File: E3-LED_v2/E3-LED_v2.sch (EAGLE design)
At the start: 4 parts

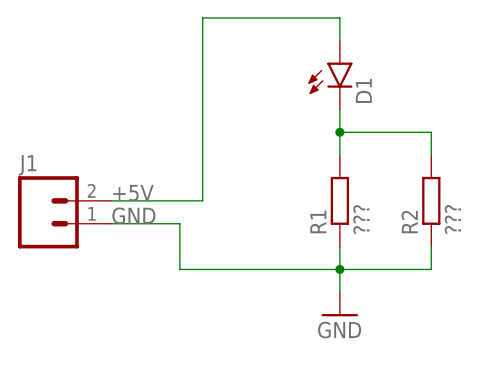
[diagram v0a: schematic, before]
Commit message: Updated BOM and schematic of v2 board with final LED and resistor choice.
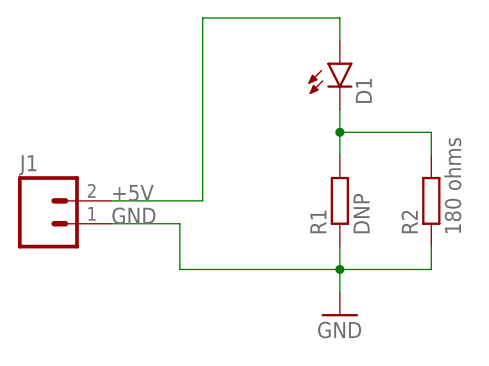
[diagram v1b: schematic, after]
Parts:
- R1: value ??? -> DNP
- R2: value ??? -> 180 ohms
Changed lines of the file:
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@@
 <grid distance="0.1" unitdist="inch" unit="inch" style="lines" multiple="1" display="no" altdistance="0.01" altunitdist="inch" altunit="inch"/>
 <layers>
-<layer number="1" name="Top" color="4" fill="1" visible="yes" active="no"/>
-<layer number="2" name="Route2" color="1" fill="3" visible="yes" active="no"/>
-<layer number="3" name="Route3" color="4" fill="3" visible="yes" active="no"/>
-<layer number="4" name="Route4" color="1" fill="4" visible="yes" active="no"/>
-<layer number="5" name="Route5" color="4" fill="4" visible="yes" active="no"/>
-<layer number="6" name="Route6" color="1" fill="8" visible="yes" active="no"/>
-<layer number="7" name="Route7" color="4" fill="8" visible="yes" active="no"/>
-<layer number="8" name="Route8" color="1" fill="2" visible="yes" active="no"/>
-<layer number="9" name="Route9" color="4" fill="2" visible="yes" active="no"/>
-<layer number="10" name="Route10" color="1" fill="7" visible="yes" active="no"/>
-<layer number="11" name="Route11" color="4" fill="7" visible="yes" active="no"/>
-<layer number="12" name="Route12" color="1" fill="5" visible="yes" active="no"/>
-<layer number="13" name="Route13" color="4" fill="5" visible="yes" active="no"/>
-<layer number="14" name="Route14" color="1" fill="6" visible="yes" active="no"/>
-<layer number="15" name="Route15" color="4" fill="6" visible="yes" active="no"/>
-<layer number="16" name="Bottom" color="1" fill="1" visible="yes" active="no"/>
-<layer number="17" name="Pads" color="2" fill="1" visible="yes" active="no"/>
-<layer number="18" name="Vias" color="2" fill="1" visible="yes" active="no"/>
-<layer number="19" name="Unrouted" color="6" fill="1" visible="yes" active="no"/>
-<layer number="20" name="Dimension" color="15" fill="1" visible="yes" active="no"/>
-<layer number="21" name="tPlace" color="7" fill="1" visible="yes" active="no"/>
-<layer number="22" name="bPlace" color="7" fill="1" visible="yes" active="no"/>
-<layer number="23" name="tOrigins" color="15" fill="1" visible="yes" active="no"/>
-<layer number="24" name="bOrigins" color="15" fill="1" visible="yes" active="no"/>
-<layer number="25" name="tNames" color="7" fill="1" visible="yes" active="no"/>
-<layer number="26" name="bNames" color="7" fill="1" visible="yes" active="no"/>
-<layer number="27" name="tValues" color="7" fill="1" visible="yes" active="no"/>
-<layer number="28" name="bValues" color="7" fill="1" visible="yes" active="no"/>
+<layer number="1" name="Top" color="4" fill="1" visible="no" active="no"/>
+<layer number="2" name="Route2" color="1" fill="3" visible="no" active="no"/>
+<layer number="3" name="Route3" color="4" fill="3" visible="no" active="no"/>
+<layer number="4" name="Route4" color="1" fill="4" visible="no" active="no"/>
+<layer number="5" name="Route5" color="4" fill="4" visible="no" active="no"/>
+<layer number="6" name="Route6" color="1" fill="8" visible="no" active="no"/>
+<layer number="7" name="Route7" color="4" fill="8" visible="no" active="no"/>
+<layer number="8" name="Route8" color="1" fill="2" visible="no" active="no"/>
+<layer number="9" name="Route9" color="4" fill="2" visible="no" active="no"/>
+<layer number="10" name="Route10" color="1" fill="7" visible="no" active="no"/>
+<layer number="11" name="Route11" color="4" fill="7" visible="no" active="no"/>
+<layer number="12" name="Route12" color="1" fill="5" visible="no" active="no"/>
+<layer number="13" name="Route13" color="4" fill="5" visible="no" active="no"/>
+<layer number="14" name="Route14" color="1" fill="6" visible="no" active="no"/>
+<layer number="15" name="Route15" color="4" fill="6" visible="no" active="no"/>
+<layer number="16" name="Bottom" color="1" fill="1" visible="no" active="no"/>
+<layer number="17" name="Pads" color="2" fill="1" visible="no" active="no"/>
+<layer number="18" name="Vias" color="2" fill="1" visible="no" active="no"/>
+<layer number="19" name="Unrouted" color="6" fill="1" visible="no" active="no"/>
+<layer number="20" name="Dimension" color="15" fill="1" visible="no" active="no"/>
+<layer number="21" name="tPlace" color="7" fill="1" visible="no" active="no"/>
+<layer number="22" name="bPlace" color="7" fill="1" visible="no" active="no"/>
+<layer number="23" name="tOrigins" color="15" fill="1" visible="no" active="no"/>
+<layer number="24" name="bOrigins" color="15" fill="1" visible="no" active="no"/>
+<layer number="25" name="tNames" color="7" fill="1" visible="no" active="no"/>
+<layer number="26" name="bNames" color="7" fill="1" visible="no" active="no"/>
+<layer number="27" name="tValues" color="7" fill="1" visible="no" active="no"/>
+<layer number="28" name="bValues" color="7" fill="1" visible="no" active="no"/>
 <layer number="29" name="tStop" color="7" fill="3" visible="no" active="no"/>
 <layer number="30" name="bStop" color="7" fill="6" visible="no" active="no"/>
@@
 <layer number="35" name="tGlue" color="7" fill="4" visible="no" active="no"/>
 <layer number="36" name="bGlue" color="7" fill="5" visible="no" active="no"/>
-<layer number="37" name="tTest" color="7" fill="1" visible="yes" active="no"/>
-<layer number="38" name="bTest" color="7" fill="1" visible="yes" active="no"/>
+<layer number="37" name="tTest" color="7" fill="1" visible="no" active="no"/>
+<layer number="38" name="bTest" color="7" fill="1" visible="no" active="no"/>
 <layer number="39" name="tKeepout" color="4" fill="11" visible="no" active="no"/>
 <layer number="40" name="bKeepout" color="1" fill="11" visible="no" active="no"/>
@@
 <layer number="44" name="Drills" color="7" fill="1" visible="no" active="no"/>
 <layer number="45" name="Holes" color="7" fill="1" visible="no" active="no"/>
-<layer number="46" name="Milling" color="3" fill="1" visible="yes" active="no"/>
-<layer number="47" name="Measures" color="7" fill="1" visible="yes" active="no"/>
-<layer number="48" name="Document" color="7" fill="1" visible="yes" active="no"/>
-<layer number="49" name="Reference" color="7" fill="1" visible="yes" active="no"/>
-<layer number="50" name="dxf" color="7" fill="1" visible="yes" active="no"/>
-<layer number="51" name="tDocu" color="7" fill="1" visible="yes" active="no"/>
-<layer number="52" name="bDocu" color="7" fill="1" visible="yes" active="no"/>
-<layer number="53" name="tGND_GNDA" color="7" fill="9" visible="yes" active="no"/>
-<layer number="54" name="bGND_GNDA" color="1" fill="9" visible="yes" active="no"/>
-<layer number="56" name="wert" color="7" fill="1" visible="yes" active="no"/>
-<layer number="57" name="tCAD" color="7" fill="1" visible="yes" active="no"/>
-<layer number="59" name="tCarbon" color="7" fill="1" visible="yes" active="no"/>
-<layer number="60" name="bCarbon" color="7" fill="1" visible="yes" active="no"/>
+<layer number="46" name="Milling" color="3" fill="1" visible="no" active="no"/>
+<layer number="47" name="Measures" color="7" fill="1" visible="no" active="no"/>
+<layer number="48" name="Document" color="7" fill="1" visible="no" active="no"/>
+<layer number="49" name="Reference" color="7" fill="1" visible="no" active="no"/>
+<layer number="50" name="dxf" color="7" fill="1" visible="no" active="no"/>
+<layer number="51" name="tDocu" color="7" fill="1" visible="no" active="no"/>
+<layer number="52" name="bDocu" color="7" fill="1" visible="no" active="no"/>
+<layer number="53" name="tGND_GNDA" color="7" fill="9" visible="no" active="no"/>
+<layer number="54" name="bGND_GNDA" color="1" fill="9" visible="no" active="no"/>
+<layer number="56" name="wert" color="7" fill="1" visible="no" active="no"/>
+<layer number="57" name="tCAD" color="7" fill="1" visible="no" active="no"/>
+<layer number="59" name="tCarbon" color="7" fill="1" visible="no" active="no"/>
+<layer number="60" name="bCarbon" color="7" fill="1" visible="no" active="no"/>
 <layer number="90" name="Modules" color="5" fill="1" visible="yes" active="yes"/>
 <layer number="91" name="Nets" color="2" fill="1" visible="yes" active="yes"/>
@@
 <parts>
 <part name="FRAME1" library="frames" deviceset="LETTER_L" device=""/>
-<part name="R1" library="eagle-ltspice" deviceset="R" device="0204/7" value="???"/>
+<part name="R1" library="eagle-ltspice" deviceset="R" device="0204/7" value="DNP"/>
 <part name="GND1" library="SparkFun-Aesthetics" deviceset="GND" device=""/>
 <part name="D1" library="SparkFun-LED" deviceset="LED" device="5MM"/>
 <part name="J1" library="SparkFun-Connectors" deviceset="M02" device="PTH"/>
-<part name="R2" library="eagle-ltspice" deviceset="R" device="R0603" value="???"/>
+<part name="R2" library="eagle-ltspice" deviceset="R" device="R0603" value="180 ohms"/>
 </parts>
 <sheets>

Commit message: Tweaked silk.
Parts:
- removed R1: DNP, eagle-ltspice:R0204/7
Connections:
- net GND: no longer R1.1
- net N$3: no longer R1.2
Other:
- moved on the sheet: R2
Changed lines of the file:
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@@
 <parts>
 <part name="FRAME1" library="frames" deviceset="LETTER_L" device=""/>
-<part name="R1" library="eagle-ltspice" deviceset="R" device="0204/7" value="DNP"/>
 <part name="GND1" library="SparkFun-Aesthetics" deviceset="GND" device=""/>
 <part name="D1" library="SparkFun-LED" deviceset="LED" device="5MM"/>
@@
 <instance part="FRAME1" gate="G$1" x="0" y="0"/>
 <instance part="FRAME1" gate="G$2" x="147.32" y="0"/>
-<instance part="R1" gate="G$1" x="83.82" y="99.06" rot="R90"/>
 <instance part="GND1" gate="1" x="83.82" y="86.36"/>
 <instance part="D1" gate="G$1" x="83.82" y="114.3"/>
 <instance part="J1" gate="G$1" x="50.8" y="96.52"/>
-<instance part="R2" gate="G$1" x="93.98" y="99.06" rot="R90"/>
+<instance part="R2" gate="G$1" x="83.82" y="99.06" rot="R90"/>
 </instances>
 <busses>
@@
 <wire x1="66.04" y1="96.52" x2="66.04" y2="91.44" width="0.1524" layer="91"/>
 <wire x1="66.04" y1="91.44" x2="83.82" y2="91.44" width="0.1524" layer="91"/>
-<pinref part="R1" gate="G$1" pin="1"/>
-<wire x1="83.82" y1="91.44" x2="83.82" y2="93.98" width="0.1524" layer="91"/>
 <pinref part="GND1" gate="1" pin="GND"/>
 <wire x1="83.82" y1="88.9" x2="83.82" y2="91.44" width="0.1524" layer="91"/>
@@
 <label x="58.42" y="96.52" size="1.778" layer="95"/>
 <pinref part="R2" gate="G$1" pin="1"/>
-<wire x1="83.82" y1="91.44" x2="93.98" y2="91.44" width="0.1524" layer="91"/>
-<wire x1="93.98" y1="91.44" x2="93.98" y2="93.98" width="0.1524" layer="91"/>
+<wire x1="83.82" y1="91.44" x2="83.82" y2="93.98" width="0.1524" layer="91"/>
 </segment>
 </net>
 <net name="N$3" class="0">
 <segment>
-<pinref part="R1" gate="G$1" pin="2"/>
 <pinref part="D1" gate="G$1" pin="C"/>
-<wire x1="83.82" y1="104.14" x2="83.82" y2="106.68" width="0.1524" layer="91"/>
 <pinref part="R2" gate="G$1" pin="2"/>
-<wire x1="83.82" y1="106.68" x2="83.82" y2="109.22" width="0.1524" layer="91"/>
-<wire x1="83.82" y1="106.68" x2="93.98" y2="106.68" width="0.1524" layer="91"/>
-<wire x1="93.98" y1="106.68" x2="93.98" y2="104.14" width="0.1524" layer="91"/>
-<junction x="83.82" y="106.68"/>
+<wire x1="83.82" y1="109.22" x2="83.82" y2="104.14" width="0.1524" layer="91"/>
 </segment>
 </net>
